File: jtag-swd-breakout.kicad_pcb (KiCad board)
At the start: 2 copper layers, 16.8 x 22.3 mm, 3 parts, among them J1 JTAG, J3 68000-103HLF, J6 DS1021-1*6SF11-B

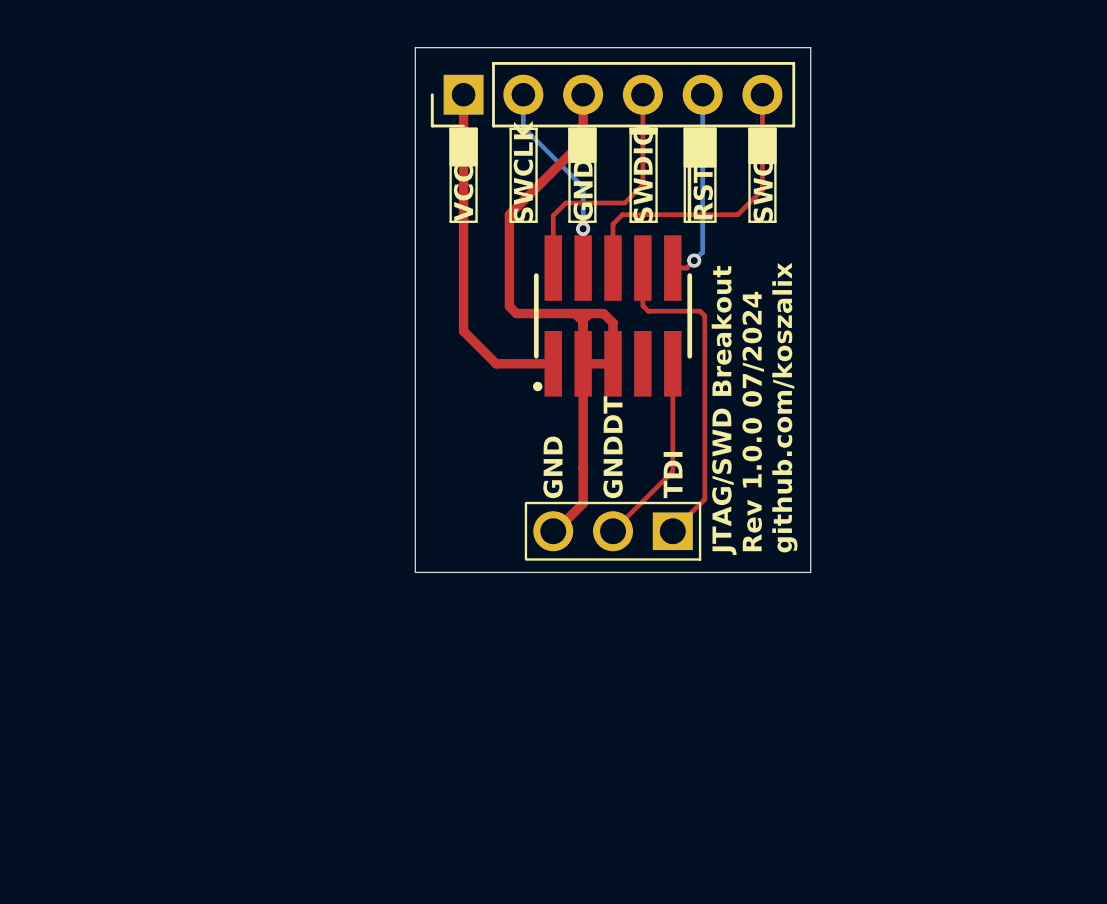
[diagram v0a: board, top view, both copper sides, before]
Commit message: Add JTAG 20
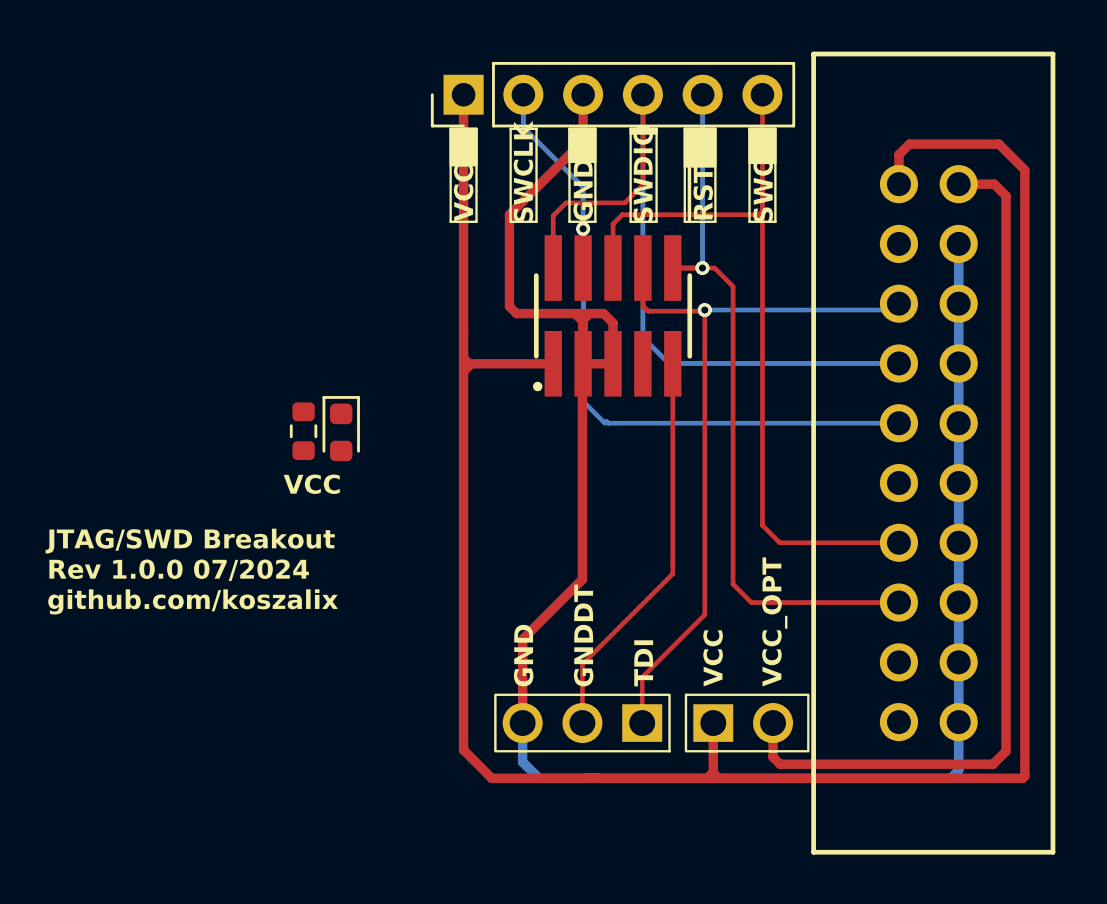
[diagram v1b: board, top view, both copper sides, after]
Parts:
- added J2: ~, Koszalix_Connectors_PinHead:SAMTEC-TST-110-01-X-D, F.Cu at (109.0, 101.4)
- added J4: 68000-102HLF, Koszalix_Connectors_PinHead:Amphenol_68000_102HLF, F.Cu at (101.2, 112.9)
- added LD1: LL-S192UGC-1B, LED_SMD:LED_0603_1608Metric, F.Cu at (83.8, 100.5)
- added R1: 1k, Resistor_SMD:R_0603_1608Metric, F.Cu at (82.2, 100.5)
- moved J3 8.25 mm to (94.1, 112.9)
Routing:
- net VCC: track 14.4 -> 92.4 mm
- net GND: track 28.7 -> 80.8 mm
- net /VCC_opt: track 0.00 -> 37.5 mm
- net /~{RST}: track 8.24 -> 31.5 mm
- net /SWDIO/TMS: track 10.4 -> 32.1 mm
- net /SWCLK/TCK: track 8.42 -> 29.6 mm
- net /SWO/TDO: track 12.9 -> 34.0 mm
- net /TDI: track 14.1 -> 31.4 mm, vias 0 -> 1
- net /GND_Detect: track 8.17 -> 16.9 mm
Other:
- board outline removed
- board text added: "VCC_OPT"

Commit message: Update adapter
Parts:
- J3: value 68000-103HLF -> DS1021-1*4SF11-B; footprint Koszalix_Connectors_PinHead:Amphenol_68000-103HLF -> Connector_PinHeader_2.54mm:PinHeader_1x04_P2.54mm_Vertical
- moved R1 9.18 mm to (88.0, 93.3)
- moved J3 7.73 mm to (89.0, 107.0), turned to 0 degrees
- moved J1 7.36 mm to (90.9, 101.4), turned to -90 degrees
- moved LD1 5.87 mm to (88.0, 96.4), turned to 90 degrees
- moved J4 4.32 mm to (100.7, 117.2)
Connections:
- J2 pad 11: unconnected-(J2-RTCK-Pad11) -> /RTCK
- J2 pad 3: unconnected-(J2-TRST-Pad3) -> /TRST
- J3 pad 1: /TDI -> /GND_Detect
- J3 pad 2: /GND_Detect -> /TDI
- J3 pad 3: GND -> /TRST
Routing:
- net /TRST: track 0.00 -> 31.9 mm, vias 0 -> 1
- net /RTCK: track 0.00 -> 23.5 mm
- net /GND_Detect: track 16.9 -> 3.16 mm
- net VCC: track 92.4 -> 97.4 mm
- net GND: track 80.8 -> 85.6 mm, vias 0 -> 3
- net /SWDIO/TMS: track 32.1 -> 28.1 mm
- net /~{RST}: track 31.5 -> 34.5 mm
- net /SWO/TDO: track 34.0 -> 31.7 mm, vias 0 -> 1
- net /VCC_opt: track 37.5 -> 39.6 mm
- net /TDI: track 31.4 -> 30.6 mm
- net /SWCLK/TCK: track 29.6 -> 30.3 mm, vias 1 -> 0
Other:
- board outline added: 29.5 x 34.1 mm
- board text added: "RTCK"
- board text added: "TRST"
- board text added: "VCCOP"
- board text removed: "VCC_OPT"
